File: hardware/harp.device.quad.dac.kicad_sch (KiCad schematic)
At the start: 0 parts

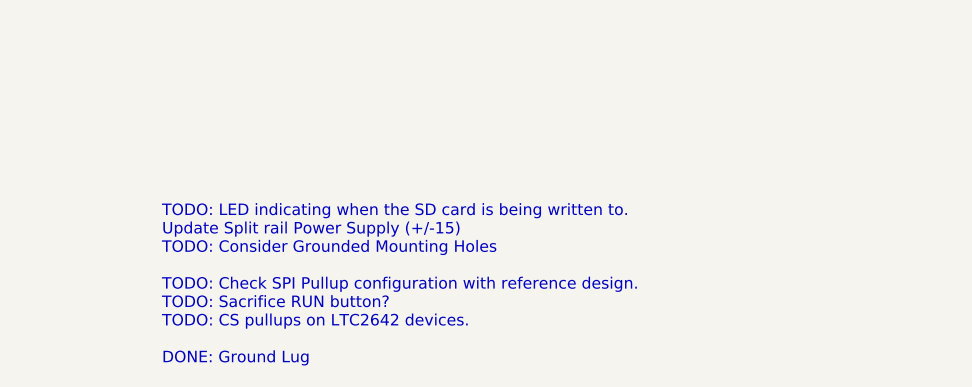
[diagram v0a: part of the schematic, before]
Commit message: fix sd card order; finish pcb draft
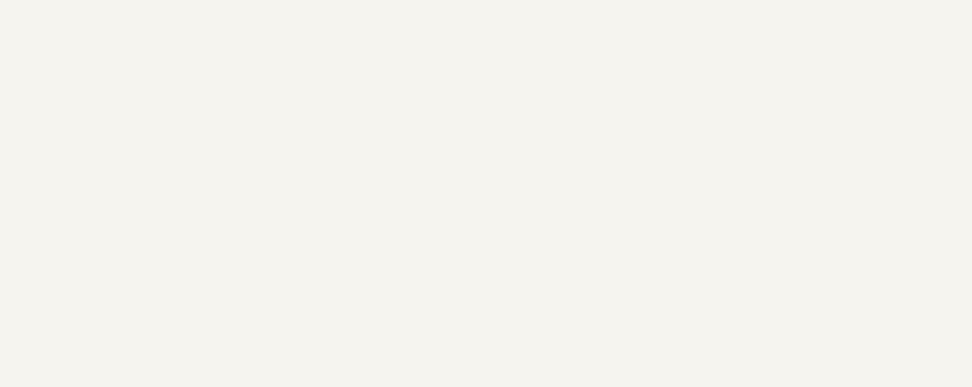
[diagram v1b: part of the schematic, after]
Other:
- note removed: "TODO: LED indicating when the SD card is being written to. Update Split rail Power Supply (+/-15) TODO: Consider Grounded Mounting Holes TODO: Check SPI Pullup configuration with reference design. TODO: Sacrifice RUN button? TODO: CS pullups on LTC2642 devices. DONE: Ground Lug"
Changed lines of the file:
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@@
 		(comment 1 "Hexabitz")
-	)
-	(text "TODO: LED indicating when the SD card is being written to.\nUpdate Split rail Power Supply (+/-15)\nTODO: Consider Grounded Mounting Holes\n\nTODO: Check SPI Pullup configuration with reference design.\nTODO: Sacrifice RUN button?\nTODO: CS pullups on LTC2642 devices.\n\nDONE: Ground Lug"
-		(exclude_from_sim no)
-		(at 96.012 127.254 0)
-		(effects
-			(font
-				(size 1.27 1.27)
-			)
-			(justify left)
-		)
 	)
 	(sheet

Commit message: update board draft
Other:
- note added: "TODO: LED indicating when the SD card is being written to. TODO: TPD8E003DQDR for EMI protection on SD card. TODO: CS pullups on LTC2642 devices. Update Split rail Power Supply (+/-15 and smaller voltage regulator) TODO: Consider Grounded Mounting Holes TODO: Ground Lug TODO: Check SPI Pullup configuration with reference design."
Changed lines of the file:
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@@
 		(comment 1 "Hexabitz")
+	)
+	(text "TODO: LED indicating when the SD card is being written to.\nTODO: TPD8E003DQDR for EMI protection on SD card.\nTODO: CS pullups on LTC2642 devices.\nUpdate Split rail Power Supply (+/-15 and smaller voltage regulator)\nTODO: Consider Grounded Mounting Holes\nTODO: Ground Lug\nTODO: Check SPI Pullup configuration with reference design."
+		(exclude_from_sim no)
+		(at 96.012 127.254 0)
+		(effects
+			(font
+				(size 1.27 1.27)
+			)
+			(justify left)
+		)
 	)
 	(sheet

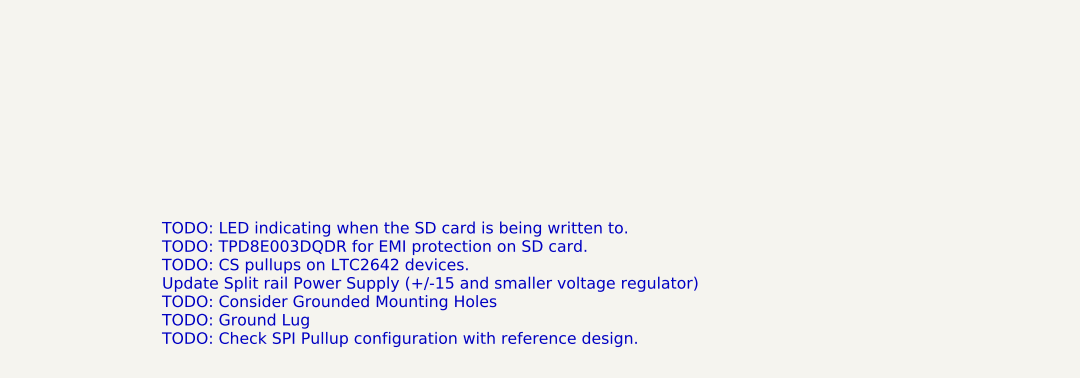
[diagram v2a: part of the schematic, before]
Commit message: draft power pours in internal layers
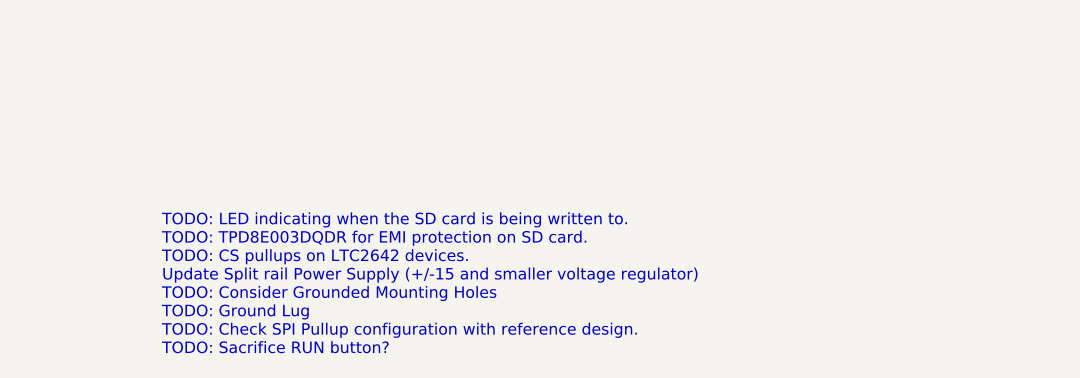
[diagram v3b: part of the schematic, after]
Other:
- note added: "TODO: LED indicating when the SD card is being written to. TODO: TPD8E003DQDR for EMI protection on SD card. TODO: CS pullups on LTC2642 devices. Update Split rail Power Supply (+/-15 and smaller voltage regulator) TODO: Consider Grounded Mounting Holes TODO: Ground Lug TODO: Check SPI Pullup configuration with reference design. TODO: Sacrifice RUN button?"
- note removed: "TODO: LED indicating when the SD card is being written to. TODO: TPD8E003DQDR for EMI protection on SD card. TODO: CS pullups on LTC2642 devices. Update Split rail Power Supply (+/-15 and smaller voltage regulator) TODO: Consider Grounded Mounting Holes TODO: Ground Lug TODO: Check SPI Pullup configuration with reference design."
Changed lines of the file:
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@@
 		(comment 1 "Hexabitz")
 	)
-	(text "TODO: LED indicating when the SD card is being written to.\nTODO: TPD8E003DQDR for EMI protection on SD card.\nTODO: CS pullups on LTC2642 devices.\nUpdate Split rail Power Supply (+/-15 and smaller voltage regulator)\nTODO: Consider Grounded Mounting Holes\nTODO: Ground Lug\nTODO: Check SPI Pullup configuration with reference design."
+	(text "TODO: LED indicating when the SD card is being written to.\nTODO: TPD8E003DQDR for EMI protection on SD card.\nTODO: CS pullups on LTC2642 devices.\nUpdate Split rail Power Supply (+/-15 and smaller voltage regulator)\nTODO: Consider Grounded Mounting Holes\nTODO: Ground Lug\nTODO: Check SPI Pullup configuration with reference design.\nTODO: Sacrifice RUN button?"
 		(exclude_from_sim no)
 		(at 96.012 127.254 0)

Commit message: update pcb draft
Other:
- note added: "TODO: LED indicating when the SD card is being written to. Update Split rail Power Supply (+/-15) TODO: Consider Grounded Mounting Holes TODO: Check SPI Pullup configuration with reference design. TODO: Sacrifice RUN button? TODO: CS pullups on LTC2642 devices. DONE: Ground Lug"
- note removed: "TODO: LED indicating when the SD card is being written to. TODO: TPD8E003DQDR for EMI protection on SD card. TODO: CS pullups on LTC2642 devices. Update Split rail Power Supply (+/-15 and smaller voltage regulator) TODO: Consider Grounded Mounting Holes TODO: Ground Lug TODO: Check SPI Pullup configuration with reference design. TODO: Sacrifice RUN button?"
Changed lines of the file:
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@@
 		(comment 1 "Hexabitz")
 	)
-	(text "TODO: LED indicating when the SD card is being written to.\nTODO: TPD8E003DQDR for EMI protection on SD card.\nTODO: CS pullups on LTC2642 devices.\nUpdate Split rail Power Supply (+/-15 and smaller voltage regulator)\nTODO: Consider Grounded Mounting Holes\nTODO: Ground Lug\nTODO: Check SPI Pullup configuration with reference design.\nTODO: Sacrifice RUN button?"
+	(text "TODO: LED indicating when the SD card is being written to.\nUpdate Split rail Power Supply (+/-15)\nTODO: Consider Grounded Mounting Holes\n\nTODO: Check SPI Pullup configuration with reference design.\nTODO: Sacrifice RUN button?\nTODO: CS pullups on LTC2642 devices.\n\nDONE: Ground Lug"
 		(exclude_from_sim no)
 		(at 96.012 127.254 0)
